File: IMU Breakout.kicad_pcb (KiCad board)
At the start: 2 copper layers, 20 x 20 mm, 15 parts, among them J1 Conn_01x06_Male, U1 STM32L432KCUx, U2 BNO055, U3 MIC5501-3.0YM5, Y1 32MHZ, Y2 Crystal

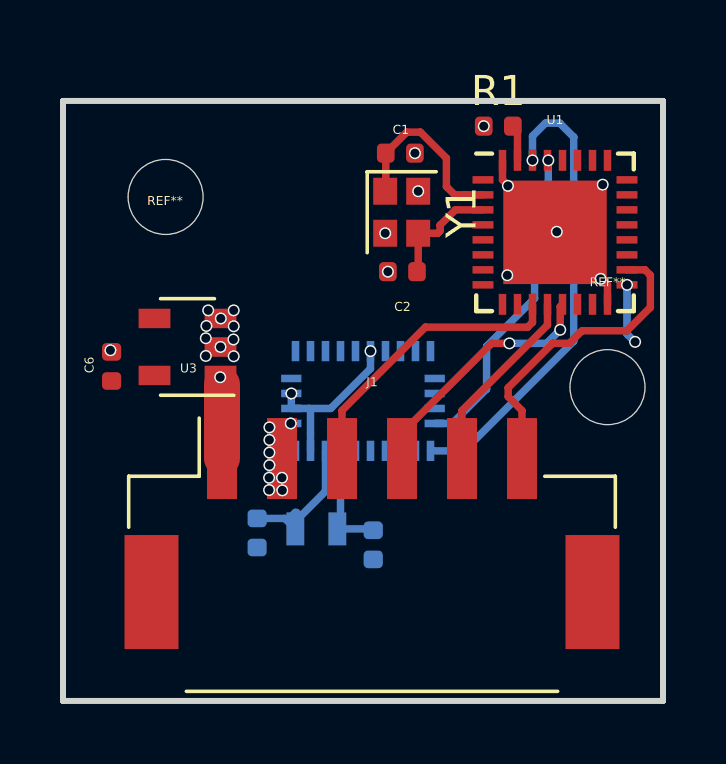
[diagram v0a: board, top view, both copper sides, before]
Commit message: added uart and programming
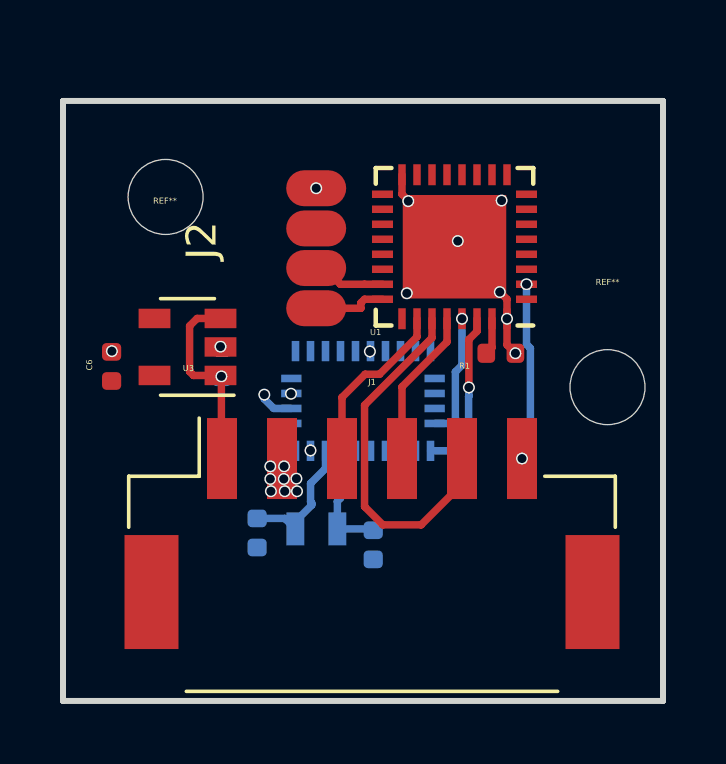
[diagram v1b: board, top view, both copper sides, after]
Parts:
- removed C1, C2: 10PF, Capacitor_SMD:C_0402_1005Metric
- removed Y1: 32MHZ, Crystal:Crystal_SMD_2016-4Pin_2.0x1.6mm
- added J2: Conn_01x04_Female, pads1x4:1x4Pads, F.Cu at (8.44, 4.91)
- moved R1 7.57 mm to (14.6, 8.41), turned to 180 degrees
- moved U1 3.38 mm to (13.1, 4.86), turned to 180 degrees
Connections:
- U1 pad 11: SCK -> (no net)
- U1 pad 12: MISO -> (no net)
- U1 pad 13: MOSI -> (no net)
- U1 pad 18: CS -> (no net)
- U1 pad 2: Net-(C1-Pad2) -> CS
- U1 pad 23: (no net) -> SWDIO
- U1 pad 24: (no net) -> SWCLK
- U1 pad 26: (no net) -> SCK
- U1 pad 27: (no net) -> MISO
- U1 pad 28: (no net) -> MOSI
- U1 pad 3: Net-(C2-Pad1) -> (no net)
- U3 pad 3: GND -> +BATT
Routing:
- net SDA: track 15.6 -> 5.43 mm
- net +3V3: track 7.72 -> 1.18 mm
- net SCL: track 10.7 -> 4.23 mm
- net Net-(C1-Pad2): track 6.42 -> 0.00 mm
- net MISO: track 6.32 -> 12.1 mm
- net CS: track 11.2 -> 5.98 mm, vias 0 -> 2
- net +BATT: track 2.48 -> 6.49 mm
- net Net-(C2-Pad1): track 3.89 -> 0.00 mm
- net SCK: track 9.77 -> 5.98 mm
- net MOSI: track 8.43 -> 5.28 mm, vias 2 -> 0
- net SWCLK: track 0.00 -> 2.44 mm
- net SWDIO: track 0.00 -> 2.43 mm
- net GND: track 6.25 -> 7.52 mm, vias 30 -> 18
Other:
- net class Power: trace_width 1.2 -> 0.25
- board text added: "Keion Bisland Xavier Little Alex Tacescu"
- board text added: "SmallKat MQP IMU Breakout Rev 1"
